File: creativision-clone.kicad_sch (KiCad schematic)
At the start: 20 parts, among them SW1 Reset, U1 6821, U12 74LS32, U15 74LS139, U2 SN76489AN, U3 6502, U4 TMS9918A, U5 27256, U6 AS6C62256-DIP, X1 2MHz

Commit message: VDP train, WRAM RD
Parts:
- added C2: 0.1µF, symbol Device:C_Small
- added R15, R16, R17, R18, R57, R58: 3.3kΩ, symbol Device:R_Small_US
- added U1: AS6C62256-DIP, Housings_DIP:DIP-28_W15.24mm_Socket_LongPads, symbol AS6C62256:AS6C62256-DIP
- added U100, U101, U102: 74HCT574, symbol 74xx:74HCT574
- added U99: 74HCT04, symbol 74xx:74HCT04
- renumbered U6 to U18, U3 to U2, U5 to U20, U1 to U21, U2 to U22, U4 to U3
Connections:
- net +5V: now also U21.20 (VCC), U21.22 (CS0), U21.24 (CS1), U22.16 (Vcc), U3.33 (VCC), C2.1, R15.1, R16.1, R17.1, R18.1, R57.1, R58.1, U1.28 (Vcc), U100.20 (VCC), U101.20 (VCC), U102.20 (VCC), U99.14 (VCC)
- net GND: now also U21.1 (VSS), U22.8 (GND), U3.12 (GND), C2.2, U1.1 (A14), U1.14 (GND), U100.10 (GND), U101.1 (OE), U101.10 (GND), U102.1 (OE), U102.10 (GND), U99.7 (GND)
- net R/~{W}: now also U21.21 (R/~{W})
- net a0: now also U21.36 (RS0)
- net a1: now also U21.35 (RS1)
- net d0: now also U21.33 (D0)
- net d1: now also U21.32 (D1)
- net d2: now also U21.31 (D2)
- net d3: now also U21.30 (D3)
- net d4: now also U21.29 (D4)
- net d5: now also U21.28 (D5)
- net d6: now also U21.27 (D6)
- net d7: now also U21.26 (D7)
- net ~{PIA}: now also U21.23 (~{CS2})
- net ~{RESET}: now also U21.34 (~{RESET}), U3.34 (~{RESET})
- net Φ2: now reaches U2.39 (ϕ2)
- net Φ2: now also U21.25 (ENABLE), U22.14 (CLK)
- net at U21.18 (CB1): now also U22.4 (READY), U22.5 (~{WE}), R58.2
- net at U21.19 (CB2): now also U22.6 (~{CE}), R57.2
- net at U21.37 (~{IRQB}): now also R15.2
- net at U21.38 (~{IRQA}): now also R16.2
- net at U21.39 (CA2): now also R17.2
- net at U21.40 (CA1): now also R18.2
- net ~{WRAM_OE}: now reaches U18.22 (~{OE})
- net ~{WRAM_OE}: now also U99.12
- net ~{WRAM_WE}: now reaches U12.6, U18.27 (~{WE})
- net ~{WRAM_WE}: now also U99.13
- net ~{VDP_RAS}: now reaches U3.1 (~{RAS})
- net ~{VDP_RAS}: now also U99.3
- net ad0: now reaches U3.10 (AD0)
- net ad0: now also U100.2 (D0), U101.2 (D0), U102.2 (D0)
- net VDP_R~{W}: now reaches U3.11 (R/~{W})
- net VDP_R~{W}: now also U1.27 (~{WE}), U100.1 (OE), U99.1
- net ~{VDP_CAS}: now reaches U3.2 (~{CAS})
- net ~{VDP_CAS}: now also U1.20 (~{CE}), U99.5
- net vd7: now reaches U3.25 (RD7)
- net vd7: now also U1.19 (DQ7), U100.12 (Q7)
- net vd6: now reaches U3.26 (RD6)
- net vd6: now also U1.18 (DQ6), U100.13 (Q6)
- net vd5: now reaches U3.27 (RD5)
- net vd5: now also U1.17 (DQ5), U100.14 (Q5)
- net vd4: now reaches U3.28 (RD4)
- net vd4: now also U1.16 (DQ4), U100.15 (Q4)
- net vd3: now reaches U3.29 (RD3)
- net vd3: now also U1.15 (DQ3), U100.16 (Q3)
- net ad7: now reaches U3.3 (AD7)
- net ad7: now also U100.9 (D7), U101.9 (D7), U102.9 (D7)
- net vd2: now reaches U3.30 (RD2)
- net vd2: now also U1.13 (DQ2), U100.17 (Q2)
- net vd1: now reaches U3.31 (RD1)
- net vd1: now also U1.12 (DQ1), U100.18 (Q1)
- net vd0: now reaches U3.32 (RD0)
- net vd0: now also U1.11 (DQ0), U100.19 (Q0)
- net ad6: now reaches U3.4 (AD6)
- net ad6: now also U100.8 (D6), U101.8 (D6), U102.8 (D6)
- net ad5: now reaches U3.5 (AD5)
- net ad5: now also U100.7 (D5), U101.7 (D5), U102.7 (D5)
- net ad4: now reaches U3.6 (AD4)
- net ad4: now also U100.6 (D4), U101.6 (D4), U102.6 (D4)
- net ad3: now reaches U3.7 (AD3)
- net ad3: now also U100.5 (D3), U101.5 (D3), U102.5 (D3)
- net ad2: now reaches U3.8 (AD2)
- net ad2: now also U100.4 (D2), U101.4 (D2), U102.4 (D2)
- net ad1: now reaches U3.9 (AD1)
- net ad1: now also U100.3 (D1), U101.3 (D1), U102.3 (D1)
- new net: U99.6, U99.9
- new net: U99.11, U99.8
- new net VDP_W~{R}: U1.22 (~{OE}), U100.11 (Cp), U99.2
- new net VRAM_COL: U102.11 (Cp), U99.10
- new net VRAM_ROW: U101.11 (Cp), U99.4
- new net vram_a0: U1.10 (A0), U101.18 (Q1)
- new net vram_a1: U1.9 (A1), U101.17 (Q2)
- new net vram_a10: U1.24 (A9), U102.15 (Q4)
- new net vram_a11: U1.2 (A12), U102.14 (Q5)
- new net vram_a12: U1.25 (A8), U102.13 (Q6)
- new net vram_a13: U1.26 (A13), U102.12 (Q7)
- new net vram_a2: U1.8 (A2), U101.16 (Q3)
- new net vram_a3: U1.7 (A3), U101.15 (Q4)
- new net vram_a4: U1.21 (A10), U101.14 (Q5)
- new net vram_a5: U1.6 (A4), U101.13 (Q6)
- new net vram_a6: U1.5 (A5), U101.12 (Q7)
- new net vram_a7: U1.23 (A11), U102.18 (Q1)
- new net vram_a8: U1.4 (A6), U102.17 (Q2)
- new net vram_a9: U1.3 (A7), U102.16 (Q3)
- no-connect marks 4 -> 8
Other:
- note added: "PIA"
- note added: "TODO: Clock"
- note added: "TODO: Keyboard mess"
- note added: "TODO: P1, pin 26"
- note added: "TODO: Video out amplification"
- note added: "TODO: Wire up audio out"
- note added: "TODO: wire up PB, PA to this"
- note added: "VDP"
- note removed: "TODO: ~{OE} Read signal (original is 2114, where /WE=1, /CS=0 means read and /WE=0, /CS=0 means write)"
- moved on the sheet: U21, U22

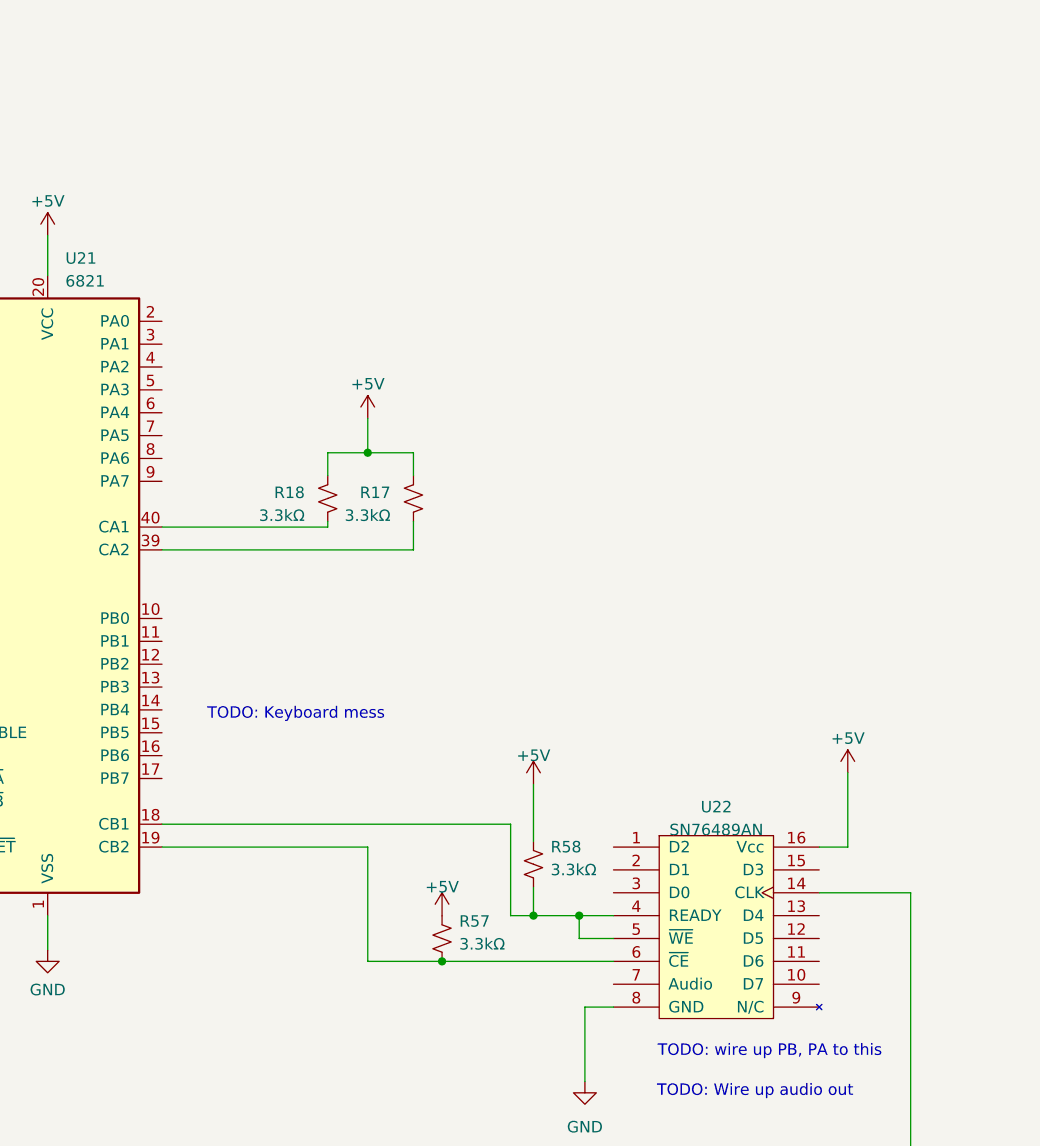
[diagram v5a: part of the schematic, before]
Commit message: keyboard matrix
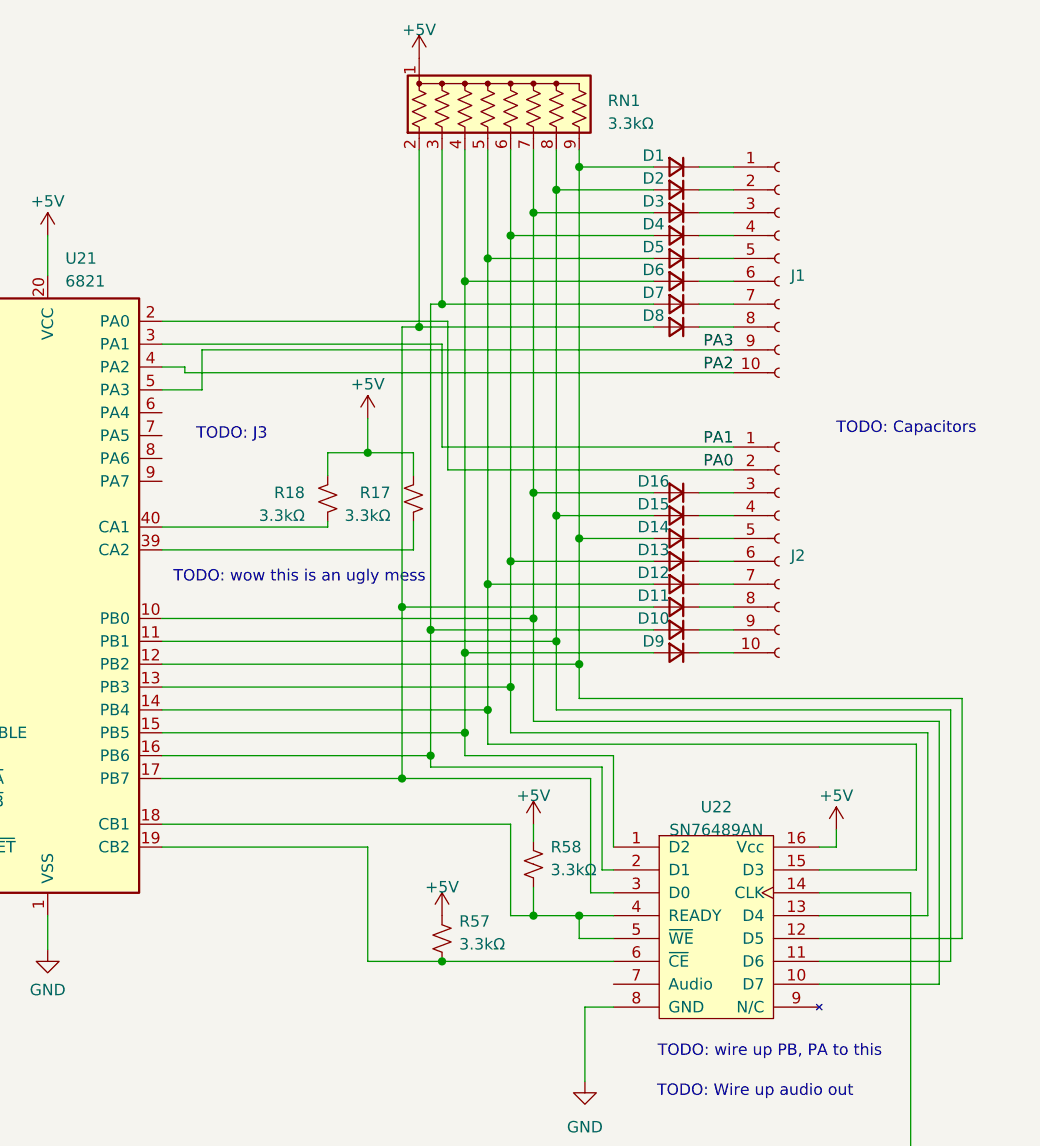
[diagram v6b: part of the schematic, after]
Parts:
- added D1, D10, D11, D12, D13, D14, D15, D16, D2, D3, D4, D5, D6, D7, D8, D9: D_Small, symbol Device:D_Small
- added J1, J2: Conn_01x10_Socket, symbol Connector:Conn_01x10_Socket
- added RN1: 3.3kΩ, Resistor_THT:R_Array_SIP9, symbol Device:R_Network08_US
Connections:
- net +5V: now also RN1.1 (common)
- net at U21.10 (PB0): now also U22.10 (D7), D16.2 (A), D3.2 (A), RN1.7 (R6)
- net at U21.11 (PB1): now also U22.11 (D6), D15.2 (A), D2.2 (A), RN1.8 (R7)
- net at U21.12 (PB2): now also U22.12 (D5), D1.2 (A), D14.2 (A), RN1.9 (R8)
- net at U21.13 (PB3): now also U22.13 (D4), D13.2 (A), D4.2 (A), RN1.6 (R5)
- net at U21.14 (PB4): now also U22.15 (D3), D12.2 (A), D5.2 (A), RN1.5 (R4)
- net at U21.15 (PB5): now also U22.1 (D2), D6.2 (A), D9.2 (A), RN1.4 (R3)
- net at U21.16 (PB6): now also U22.2 (D1), D10.2 (A), D7.2 (A), RN1.3 (R2)
- net at U21.17 (PB7): now also U22.3 (D0), D11.2 (A), D8.2 (A), RN1.2 (R1)
- net PA0: now reaches U21.2 (PA0)
- net PA0: now also J2.2 (Pin_2)
- net PA1: now reaches U21.3 (PA1)
- net PA1: now also J2.1 (Pin_1)
- net PA2: now reaches U21.4 (PA2)
- net PA2: now also J1.10 (Pin_10)
- net PA3: now reaches U21.5 (PA3)
- net PA3: now also J1.9 (Pin_9)
- new net: D3.1 (K), J1.3 (Pin_3)
- new net: D2.1 (K), J1.2 (Pin_2)
- new net: D6.1 (K), J1.6 (Pin_6)
- new net: D7.1 (K), J1.7 (Pin_7)
- new net: D16.1 (K), J2.3 (Pin_3)
- new net: D8.1 (K), J1.8 (Pin_8)
- new net: D12.1 (K), J2.7 (Pin_7)
- new net: D14.1 (K), J2.5 (Pin_5)
- new net: D1.1 (K), J1.1 (Pin_1)
- new net: D4.1 (K), J1.4 (Pin_4)
- new net: D5.1 (K), J1.5 (Pin_5)
- new net: D10.1 (K), J2.9 (Pin_9)
- new net: D9.1 (K), J2.10 (Pin_10)
- new net: D11.1 (K), J2.8 (Pin_8)
- new net: D13.1 (K), J2.6 (Pin_6)
- new net: D15.1 (K), J2.4 (Pin_4)
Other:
- note added: "TODO: Capacitors"
- note added: "TODO: J3"
- note added: "TODO: wow this is an ugly mess"
- note removed: "TODO: Keyboard mess"

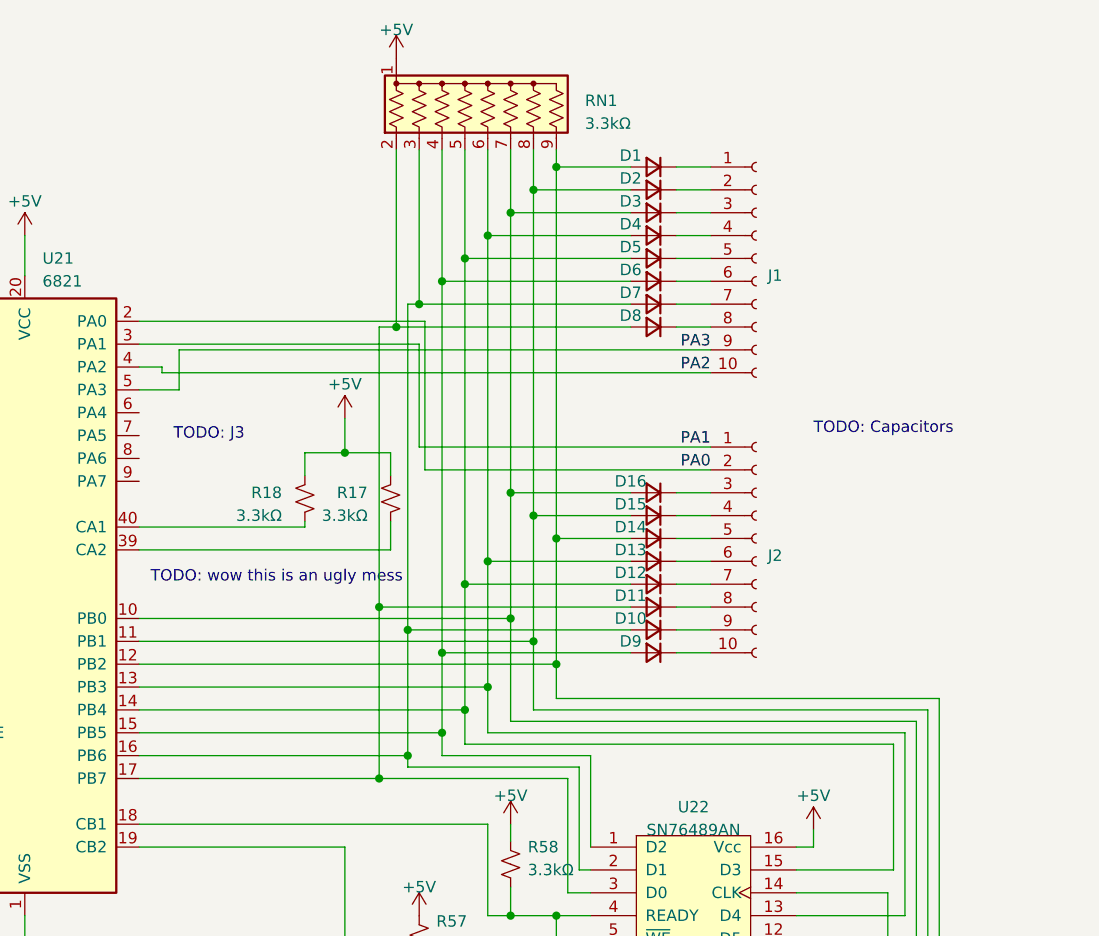
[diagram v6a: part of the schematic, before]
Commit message: Second half of keyboard matrix
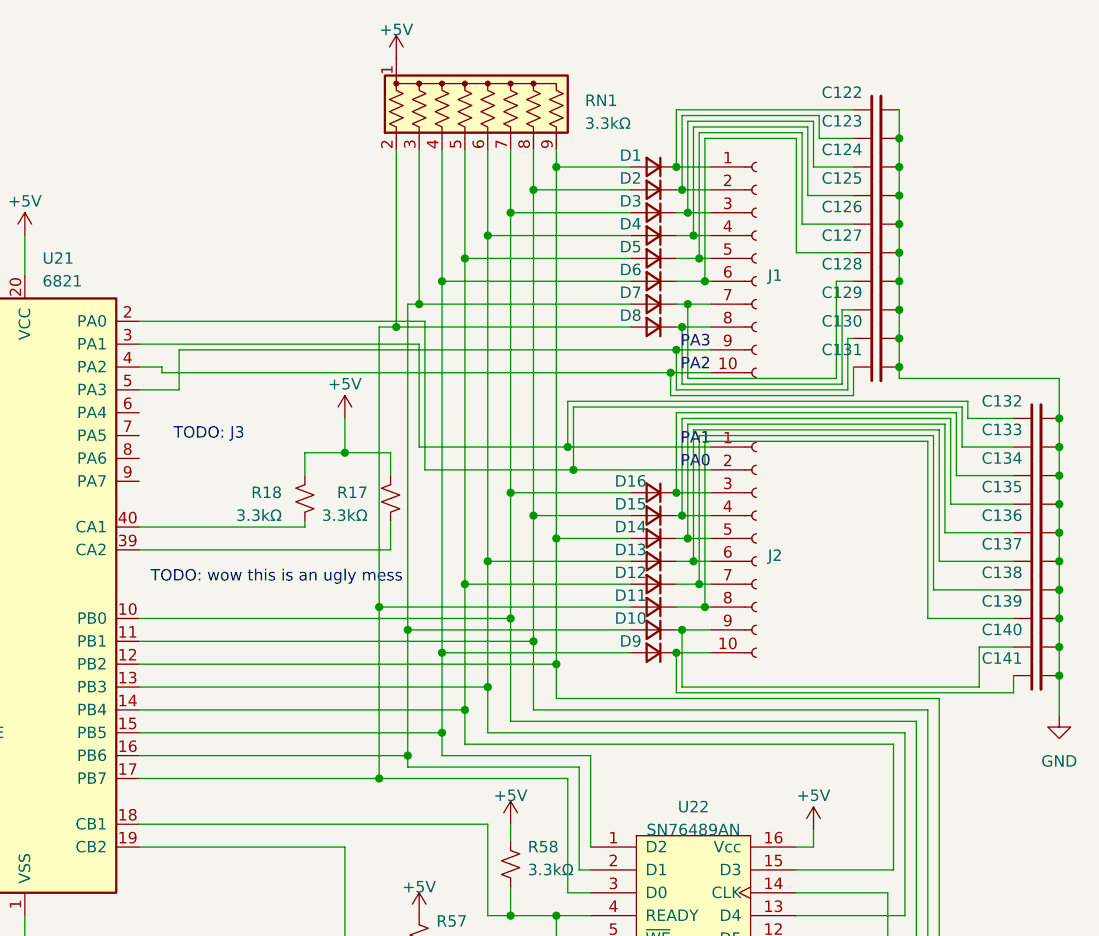
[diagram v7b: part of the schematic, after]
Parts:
- added C122, C123, C124, C125, C126, C127, C128, C129, C130, C131, C132, C133, C134, C135, C136, C137, C138, C139, C140, C141: C_Small, symbol Device:C_Small
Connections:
- net GND: now also C122.2, C123.2, C124.2, C125.2, C126.2, C127.2, C128.2, C129.2, C130.2, C131.2, C132.2, C133.2, C134.2, C135.2, C136.2, C137.2, C138.2, C139.2, C140.2, C141.2
- net PA0: now also C133.1
- net PA1: now also C132.1
- net PA2: now also C131.1
- net PA3: now also C130.1
- net at D3.1 (K), J1.3 (Pin_3): now also C124.1
- net at D2.1 (K), J1.2 (Pin_2): now also C123.1
- net at D6.1 (K), J1.6 (Pin_6): now also C127.1
- net at D7.1 (K), J1.7 (Pin_7): now also C128.1
- net at D16.1 (K), J2.3 (Pin_3): now also C134.1
- net at D8.1 (K), J1.8 (Pin_8): now also C129.1
- net at D12.1 (K), J2.7 (Pin_7): now also C138.1
- net at D14.1 (K), J2.5 (Pin_5): now also C136.1
- net at D1.1 (K), J1.1 (Pin_1): now also C122.1
- net at D4.1 (K), J1.4 (Pin_4): now also C125.1
- net at D5.1 (K), J1.5 (Pin_5): now also C126.1
- net at D10.1 (K), J2.9 (Pin_9): now also C140.1
- net at D9.1 (K), J2.10 (Pin_10): now also C141.1
- net at D11.1 (K), J2.8 (Pin_8): now also C139.1
- net at D13.1 (K), J2.6 (Pin_6): now also C137.1
- net at D15.1 (K), J2.4 (Pin_4): now also C135.1
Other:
- note removed: "TODO: Capacitors"
